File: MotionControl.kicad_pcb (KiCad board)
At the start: 2 copper layers, 29 parts, among them J1 Screw_Terminal_01x02, J2 Conn_ARM_JTAG_SWD_10, P1 USB_C_Plug_USB2.0, SW1 SW_Push, U1 ATSAMD21J18A-A, U2 AP2112K-3.3, Y1 32.768kHz

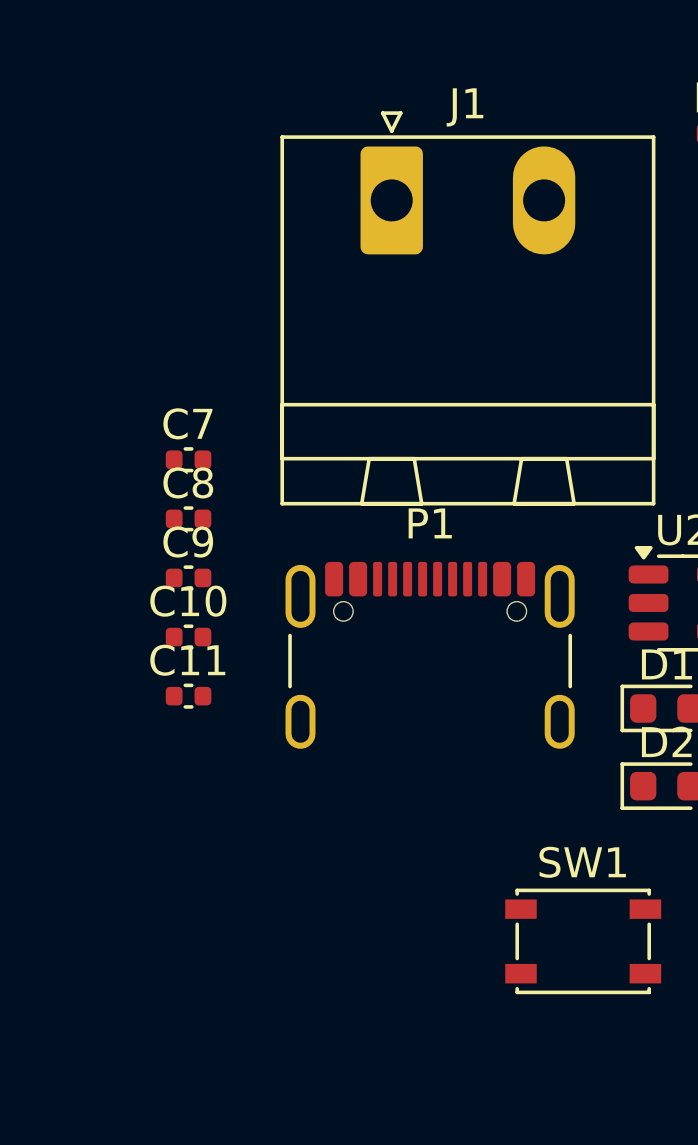
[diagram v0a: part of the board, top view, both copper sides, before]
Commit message: tx, rx leds
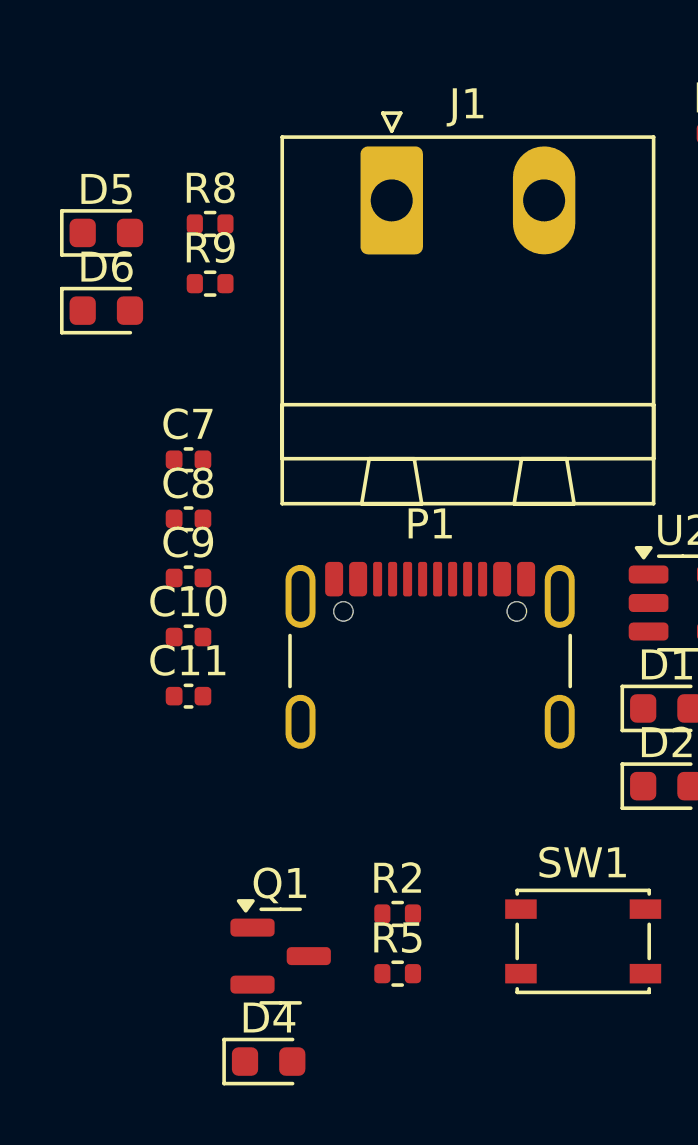
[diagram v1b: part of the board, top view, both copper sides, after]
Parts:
- added D4: Blue, LED_SMD:LED_0603_1608Metric, F.Cu at (125.4, 123.7)
- added D5: Green, LED_SMD:LED_0603_1608Metric, F.Cu at (120.0, 96.1)
- added D6: Yellow, LED_SMD:LED_0603_1608Metric, F.Cu at (120.0, 98.7)
- added Q1: 2N7002, Package_TO_SOT_SMD:SOT-23, F.Cu at (125.8, 120.2)
- added R2: 10R, Resistor_SMD:R_0402_1005Metric, F.Cu at (129.7, 118.8)
- added R5: 100K, Resistor_SMD:R_0402_1005Metric, F.Cu at (129.7, 120.8)
- added R8: 130R, Resistor_SMD:R_0402_1005Metric, F.Cu at (123.5, 95.8)
- added R9: 130R, Resistor_SMD:R_0402_1005Metric, F.Cu at (123.5, 97.8)
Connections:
- U1 pad 36: unconnected-(U1-PA17-Pad36) -> PA17_LED
- U1 pad 51: unconnected-(U1-PA27-Pad51) -> PA27_TX_LED
- U1 pad 64: unconnected-(U1-PB03-Pad64) -> PB03_RX_LED

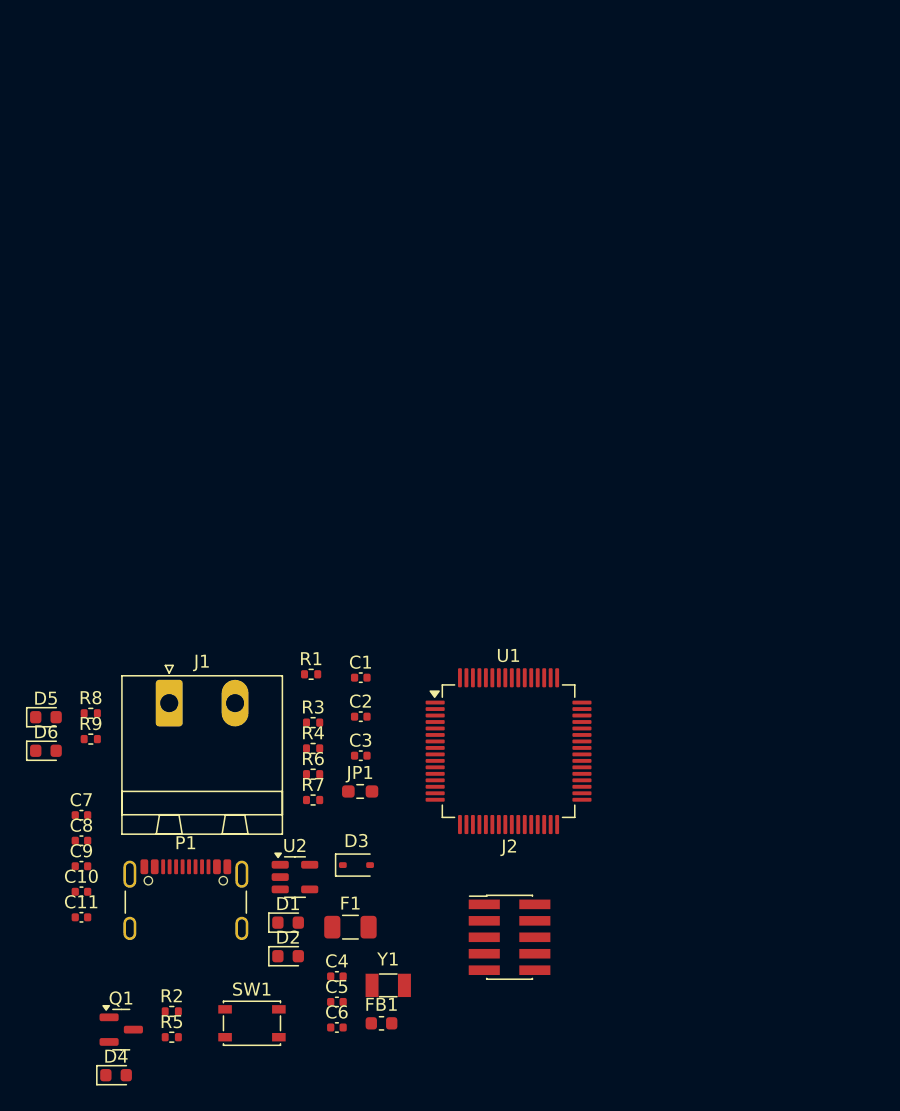
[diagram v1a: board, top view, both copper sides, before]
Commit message: Stepper unit
Made first revision for stepper unit
Contains TMC5160, Status LED, FETs, and complementary comps
Will be x4 later
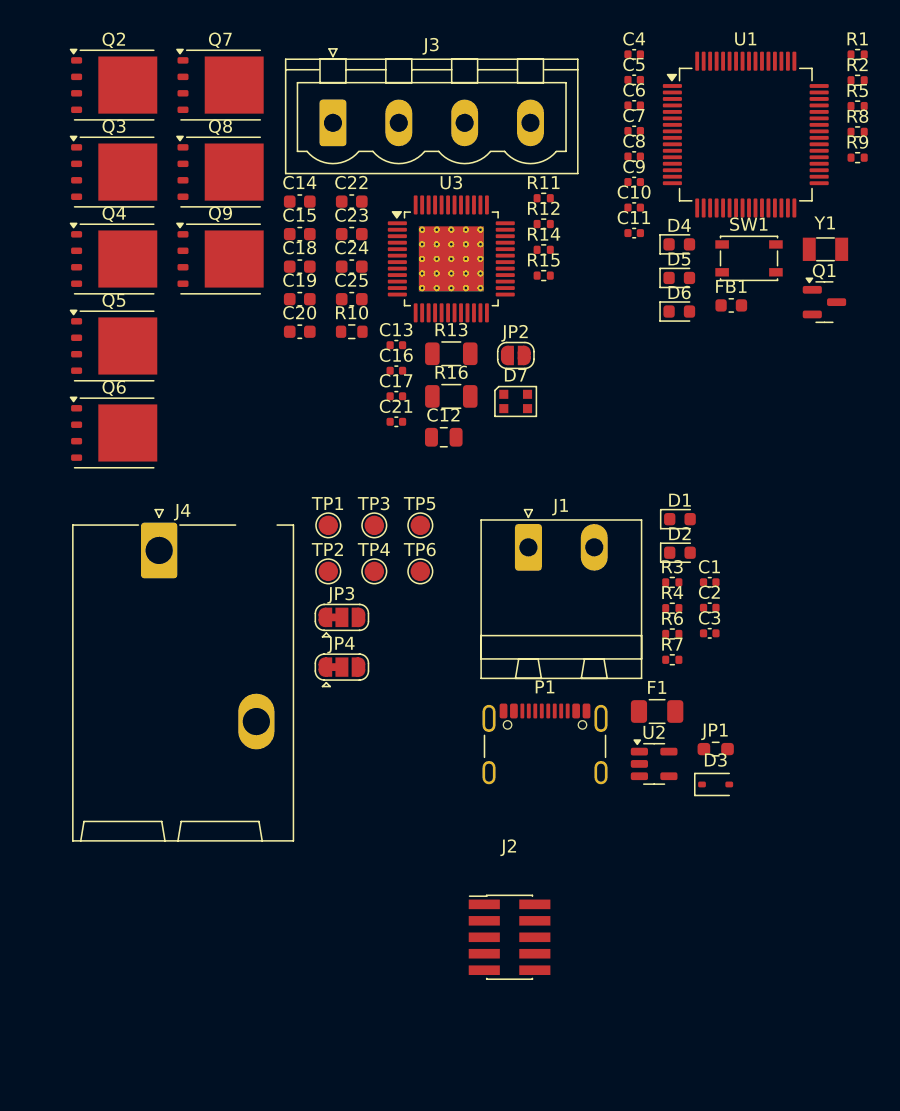
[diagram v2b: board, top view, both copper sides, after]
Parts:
- added C12: 10uF 50V, Capacitor_SMD:C_0805_2012Metric, F.Cu at (150.7, 74.5)
- added C13: 22nF 50V, Capacitor_SMD:C_0402_1005Metric, F.Cu at (147.1, 67.4)
- added C14: 100nF 50V, Capacitor_SMD:C_0603_1608Metric, F.Cu at (139.6, 56.3)
- added C15: 100nF 50V, Capacitor_SMD:C_0603_1608Metric, F.Cu at (139.6, 58.8)
- added C16: 470nF 10V, Capacitor_SMD:C_0402_1005Metric, F.Cu at (147.1, 69.3)
- added C17: 4.7uF 6.3V, Capacitor_SMD:C_0402_1005Metric, F.Cu at (147.1, 71.3)
- added C18: 2.2uF 25V, Capacitor_SMD:C_0603_1608Metric, F.Cu at (139.6, 61.3)
- added C19: 100nF 50V, Capacitor_SMD:C_0603_1608Metric, F.Cu at (139.6, 63.8)
- added C20: 100nF 50V, Capacitor_SMD:C_0603_1608Metric, F.Cu at (139.6, 66.3)
- added C21: 0.1uF, Capacitor_SMD:C_0402_1005Metric, F.Cu at (147.1, 73.3)
- added C22: 100nF 50V, Capacitor_SMD:C_0603_1608Metric, F.Cu at (143.6, 56.3)
- added C23: 100nF 50V, Capacitor_SMD:C_0603_1608Metric, F.Cu at (143.6, 58.8)
- added C24: 100nF 50V, Capacitor_SMD:C_0603_1608Metric, F.Cu at (143.6, 61.3)
- added C25: 100nF 50V, Capacitor_SMD:C_0603_1608Metric, F.Cu at (143.6, 63.8)
- added D7: WS2812B-2020, LED_SMD:LED_WS2812B-2020_PLCC4_2.0x2.0mm, F.Cu at (156.3, 71.7)
- added J3: Screw_Terminal_01x04, Connector_Phoenix_MSTB:PhoenixContact_MSTBVA_2,5_4-G-5,08_1x04_P5.08mm_Vertical, F.Cu at (142.2, 50.2)
- added J4: Screw_Terminal_01x02, Connector_Phoenix_SPT:PhoenixContact_SPT_5_2-H-7.5-ZB_1x02_P7.5mm_Horizontal, F.Cu at (128.8, 83.2)
- added JP2: Jumper_2, Jumper:SolderJumper-2_P1.3mm_Open_RoundedPad1.0x1.5mm, F.Cu at (156.3, 68.2)
- added JP3: SolderJumper_3_Bridged12, Jumper:SolderJumper-3_P1.3mm_Bridged12_RoundedPad1.0x1.5mm, F.Cu at (142.9, 88.4)
- added JP4: SolderJumper_3_Bridged12, Jumper:SolderJumper-3_P1.3mm_Bridged12_RoundedPad1.0x1.5mm, F.Cu at (142.9, 92.2)
- added Q2: CSD18533Q5A, Package_TO_SOT_SMD:TDSON-8-1, F.Cu at (125.3, 47.3)
- added Q3: CSD18533Q5A, Package_TO_SOT_SMD:TDSON-8-1, F.Cu at (125.3, 54.0)
- added Q4: CSD18533Q5A, Package_TO_SOT_SMD:TDSON-8-1, F.Cu at (125.3, 60.7)
- added Q5: CSD18533Q5A, Package_TO_SOT_SMD:TDSON-8-1, F.Cu at (125.3, 67.4)
- added Q6: CSD18533Q5A, Package_TO_SOT_SMD:TDSON-8-1, F.Cu at (125.3, 74.1)
- added Q7: CSD18533Q5A, Package_TO_SOT_SMD:TDSON-8-1, F.Cu at (133.5, 47.3)
- added Q8: CSD18533Q5A, Package_TO_SOT_SMD:TDSON-8-1, F.Cu at (133.5, 54.0)
- added Q9: CSD18533Q5A, Package_TO_SOT_SMD:TDSON-8-1, F.Cu at (133.5, 60.7)
- added R10: 2R, Resistor_SMD:R_0603_1608Metric, F.Cu at (143.6, 66.3)
- added R11: 47R, Resistor_SMD:R_0402_1005Metric, F.Cu at (158.4, 56.0)
- added R12: 47R, Resistor_SMD:R_0402_1005Metric, F.Cu at (158.4, 58.0)
- added R13: R, Resistor_SMD:R_1206_3216Metric, F.Cu at (151.3, 68.0)
- added R14: 47R, Resistor_SMD:R_0402_1005Metric, F.Cu at (158.4, 60.0)
- added R15: 47R, Resistor_SMD:R_0402_1005Metric, F.Cu at (158.4, 62.0)
- added R16: R, Resistor_SMD:R_1206_3216Metric, F.Cu at (151.3, 71.3)
- added TP1: TestPoint, TestPoint:TestPoint_Pad_D1.5mm, F.Cu at (141.8, 81.3)
- added TP2: TestPoint, TestPoint:TestPoint_Pad_D1.5mm, F.Cu at (141.8, 84.8)
- added TP3: TestPoint, TestPoint:TestPoint_Pad_D1.5mm, F.Cu at (145.4, 81.3)
- added TP4: TestPoint, TestPoint:TestPoint_Pad_D1.5mm, F.Cu at (145.4, 84.8)
- added TP5: TestPoint, TestPoint:TestPoint_Pad_D1.5mm, F.Cu at (148.9, 81.3)
- added TP6: TestPoint, TestPoint:TestPoint_Pad_D1.5mm, F.Cu at (148.9, 84.8)
- added U3: TMC5160A-TA, Package_QFP:TQFP-48-1EP_7x7mm_P0.5mm_EP5x5mm_ThermalVias, F.Cu at (151.3, 60.7)
- moved R2 89.2 mm to (182.7, 46.9)
- moved R5 89.2 mm to (182.7, 48.9)
- moved Q1 78.1 mm to (180.1, 64.0)
- moved D4 77.4 mm to (168.9, 59.6)
- moved C4 74.7 mm to (165.4, 44.9)
- moved C5 74.7 mm to (165.4, 46.9)
- moved C6 74.7 mm to (165.4, 48.9)
- moved R8 74.2 mm to (182.7, 50.9)
- moved R9 74.2 mm to (182.7, 52.9)
- moved SW1 70.4 mm to (174.3, 60.7)
- moved C7 67.9 mm to (165.4, 50.8)
- moved C8 67.9 mm to (165.4, 52.8)
- moved C10 67.9 mm to (165.4, 56.7)
- moved C11 67.9 mm to (165.4, 58.7)
- moved C9 67.9 mm to (165.4, 54.8)
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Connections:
- Q1 pad 2: Net-(D4-K) -> GND
- Q1 pad 3: GND -> Net-(D4-K)

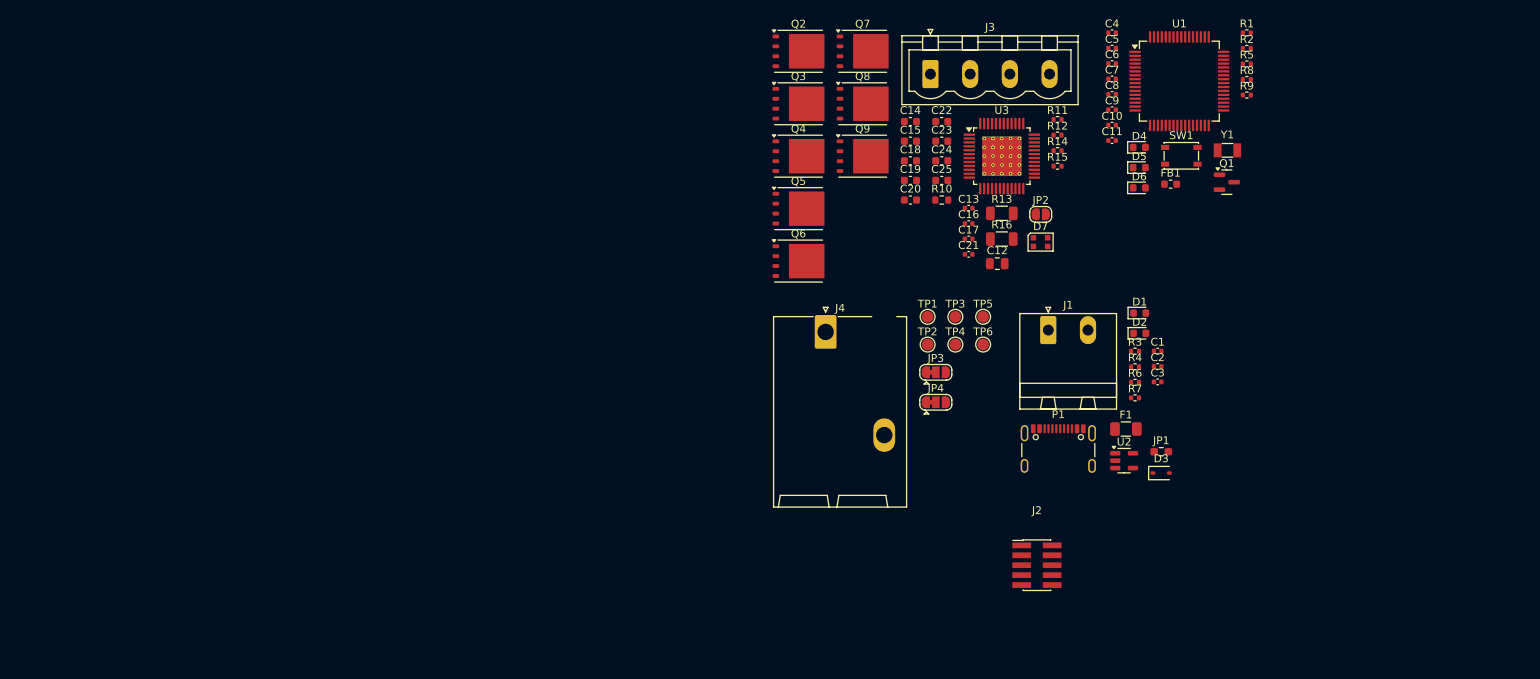
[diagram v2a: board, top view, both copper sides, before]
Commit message: x4 stepper units
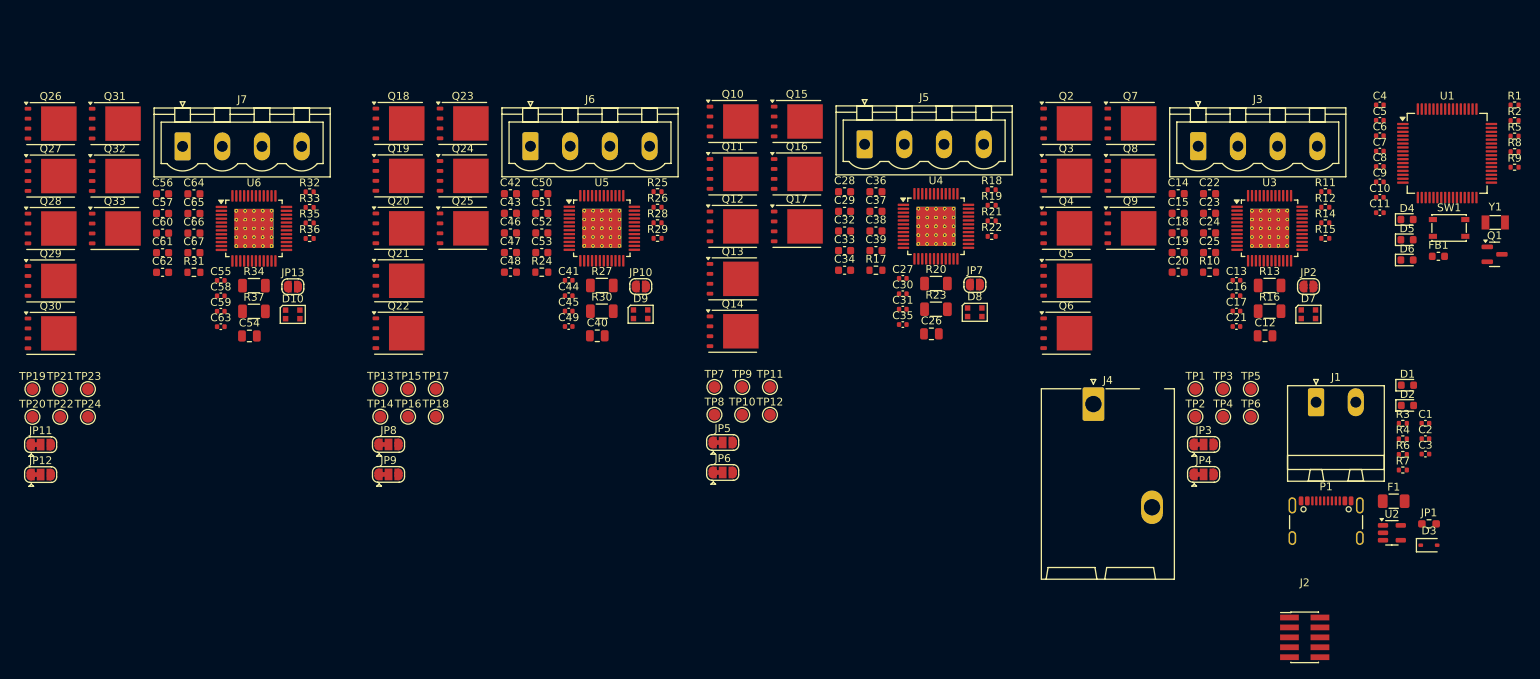
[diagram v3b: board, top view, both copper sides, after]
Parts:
- added C26: 10uF 50V, Capacitor_SMD:C_0805_2012Metric, F.Cu at (142.3, 83.4)
- added C27: 22nF 50V, Capacitor_SMD:C_0402_1005Metric, F.Cu at (138.6, 76.3)
- added C28: 100nF 50V, Capacitor_SMD:C_0603_1608Metric, F.Cu at (131.2, 65.3)
- added C29: 100nF 50V, Capacitor_SMD:C_0603_1608Metric, F.Cu at (131.2, 67.8)
- added C30: 470nF 10V, Capacitor_SMD:C_0402_1005Metric, F.Cu at (138.6, 78.3)
- added C31: 4.7uF 6.3V, Capacitor_SMD:C_0402_1005Metric, F.Cu at (138.6, 80.3)
- added C32: 2.2uF 25V, Capacitor_SMD:C_0603_1608Metric, F.Cu at (131.2, 70.3)
- added C33: 100nF 50V, Capacitor_SMD:C_0603_1608Metric, F.Cu at (131.2, 72.8)
- added C34: 100nF 50V, Capacitor_SMD:C_0603_1608Metric, F.Cu at (131.2, 75.3)
- added C35: 0.1uF, Capacitor_SMD:C_0402_1005Metric, F.Cu at (138.6, 82.2)
- added C36: 100nF 50V, Capacitor_SMD:C_0603_1608Metric, F.Cu at (135.2, 65.3)
- added C37: 100nF 50V, Capacitor_SMD:C_0603_1608Metric, F.Cu at (135.2, 67.8)
- added C38: 100nF 50V, Capacitor_SMD:C_0603_1608Metric, F.Cu at (135.2, 70.3)
- added C39: 100nF 50V, Capacitor_SMD:C_0603_1608Metric, F.Cu at (135.2, 72.8)
- added C40: 10uF 50V, Capacitor_SMD:C_0805_2012Metric, F.Cu at (99.5, 83.7)
- added C41: 22nF 50V, Capacitor_SMD:C_0402_1005Metric, F.Cu at (95.9, 76.6)
- added C42: 100nF 50V, Capacitor_SMD:C_0603_1608Metric, F.Cu at (88.4, 65.5)
- added C43: 100nF 50V, Capacitor_SMD:C_0603_1608Metric, F.Cu at (88.4, 68.0)
- added C44: 470nF 10V, Capacitor_SMD:C_0402_1005Metric, F.Cu at (95.9, 78.6)
- added C45: 4.7uF 6.3V, Capacitor_SMD:C_0402_1005Metric, F.Cu at (95.9, 80.5)
- added C46: 2.2uF 25V, Capacitor_SMD:C_0603_1608Metric, F.Cu at (88.4, 70.5)
- added C47: 100nF 50V, Capacitor_SMD:C_0603_1608Metric, F.Cu at (88.4, 73.0)
- added C48: 100nF 50V, Capacitor_SMD:C_0603_1608Metric, F.Cu at (88.4, 75.5)
- added C49: 0.1uF, Capacitor_SMD:C_0402_1005Metric, F.Cu at (95.9, 82.5)
- added C50: 100nF 50V, Capacitor_SMD:C_0603_1608Metric, F.Cu at (92.5, 65.5)
- added C51: 100nF 50V, Capacitor_SMD:C_0603_1608Metric, F.Cu at (92.5, 68.0)
- added C52: 100nF 50V, Capacitor_SMD:C_0603_1608Metric, F.Cu at (92.5, 70.5)
- added C53: 100nF 50V, Capacitor_SMD:C_0603_1608Metric, F.Cu at (92.5, 73.0)
- added C54: 10uF 50V, Capacitor_SMD:C_0805_2012Metric, F.Cu at (55.0, 83.7)
- added C55: 22nF 50V, Capacitor_SMD:C_0402_1005Metric, F.Cu at (51.4, 76.6)
- added C56: 100nF 50V, Capacitor_SMD:C_0603_1608Metric, F.Cu at (43.9, 65.5)
- added C57: 100nF 50V, Capacitor_SMD:C_0603_1608Metric, F.Cu at (43.9, 68.0)
- added C58: 470nF 10V, Capacitor_SMD:C_0402_1005Metric, F.Cu at (51.4, 78.6)
- added C59: 4.7uF 6.3V, Capacitor_SMD:C_0402_1005Metric, F.Cu at (51.4, 80.5)
- added C60: 2.2uF 25V, Capacitor_SMD:C_0603_1608Metric, F.Cu at (43.9, 70.5)
- added C61: 100nF 50V, Capacitor_SMD:C_0603_1608Metric, F.Cu at (43.9, 73.1)
- added C62: 100nF 50V, Capacitor_SMD:C_0603_1608Metric, F.Cu at (43.9, 75.6)
- added C63: 0.1uF, Capacitor_SMD:C_0402_1005Metric, F.Cu at (51.4, 82.5)
- added C64: 100nF 50V, Capacitor_SMD:C_0603_1608Metric, F.Cu at (47.9, 65.5)
- added C65: 100nF 50V, Capacitor_SMD:C_0603_1608Metric, F.Cu at (47.9, 68.0)
- added C66: 100nF 50V, Capacitor_SMD:C_0603_1608Metric, F.Cu at (47.9, 70.5)
- added C67: 100nF 50V, Capacitor_SMD:C_0603_1608Metric, F.Cu at (47.9, 73.1)
- added D10: WS2812B-2020, LED_SMD:LED_WS2812B-2020_PLCC4_2.0x2.0mm, F.Cu at (60.6, 81.0)
- added D8: WS2812B-2020, LED_SMD:LED_WS2812B-2020_PLCC4_2.0x2.0mm, F.Cu at (147.8, 80.7)
- added D9: WS2812B-2020, LED_SMD:LED_WS2812B-2020_PLCC4_2.0x2.0mm, F.Cu at (105.1, 80.9)
- added J5: Screw_Terminal_01x04, Connector_Phoenix_MSTB:PhoenixContact_MSTBVA_2,5_4-G-5,08_1x04_P5.08mm_Vertical, F.Cu at (133.8, 59.2)
- added J6: Screw_Terminal_01x04, Connector_Phoenix_MSTB:PhoenixContact_MSTBVA_2,5_4-G-5,08_1x04_P5.08mm_Vertical, F.Cu at (91.0, 59.4)
- added J7: Screw_Terminal_01x04, Connector_Phoenix_MSTB:PhoenixContact_MSTBVA_2,5_4-G-5,08_1x04_P5.08mm_Vertical, F.Cu at (46.5, 59.5)
- added JP10: Jumper_2, Jumper:SolderJumper-2_P1.3mm_Open_RoundedPad1.0x1.5mm, F.Cu at (105.1, 77.4)
- added JP11: SolderJumper_3_Bridged12, Jumper:SolderJumper-3_P1.3mm_Bridged12_RoundedPad1.0x1.5mm, F.Cu at (28.3, 97.6)
- added JP12: SolderJumper_3_Bridged12, Jumper:SolderJumper-3_P1.3mm_Bridged12_RoundedPad1.0x1.5mm, F.Cu at (28.3, 101.4)
- added JP13: Jumper_2, Jumper:SolderJumper-2_P1.3mm_Open_RoundedPad1.0x1.5mm, F.Cu at (60.6, 77.4)
- added JP5: SolderJumper_3_Bridged12, Jumper:SolderJumper-3_P1.3mm_Bridged12_RoundedPad1.0x1.5mm, F.Cu at (115.6, 97.3)
- added JP6: SolderJumper_3_Bridged12, Jumper:SolderJumper-3_P1.3mm_Bridged12_RoundedPad1.0x1.5mm, F.Cu at (115.6, 101.2)
- added JP7: Jumper_2, Jumper:SolderJumper-2_P1.3mm_Open_RoundedPad1.0x1.5mm, F.Cu at (147.9, 77.1)
- added JP8: SolderJumper_3_Bridged12, Jumper:SolderJumper-3_P1.3mm_Bridged12_RoundedPad1.0x1.5mm, F.Cu at (72.8, 97.6)
- added JP9: SolderJumper_3_Bridged12, Jumper:SolderJumper-3_P1.3mm_Bridged12_RoundedPad1.0x1.5mm, F.Cu at (72.8, 101.4)
- added Q10: CSD18533Q5A, Package_TO_SOT_SMD:TDSON-8-1, F.Cu at (116.9, 56.3)
- added Q11: CSD18533Q5A, Package_TO_SOT_SMD:TDSON-8-1, F.Cu at (116.9, 63.0)
- added Q12: CSD18533Q5A, Package_TO_SOT_SMD:TDSON-8-1, F.Cu at (116.9, 69.7)
- added Q13: CSD18533Q5A, Package_TO_SOT_SMD:TDSON-8-1, F.Cu at (116.9, 76.4)
- added Q14: CSD18533Q5A, Package_TO_SOT_SMD:TDSON-8-1, F.Cu at (116.9, 83.1)
- added Q15: CSD18533Q5A, Package_TO_SOT_SMD:TDSON-8-1, F.Cu at (125.1, 56.3)
- added Q16: CSD18533Q5A, Package_TO_SOT_SMD:TDSON-8-1, F.Cu at (125.1, 63.0)
- added Q17: CSD18533Q5A, Package_TO_SOT_SMD:TDSON-8-1, F.Cu at (125.1, 69.7)
- added Q18: CSD18533Q5A, Package_TO_SOT_SMD:TDSON-8-1, F.Cu at (74.1, 56.5)
- added Q19: CSD18533Q5A, Package_TO_SOT_SMD:TDSON-8-1, F.Cu at (74.1, 63.2)
- added Q20: CSD18533Q5A, Package_TO_SOT_SMD:TDSON-8-1, F.Cu at (74.1, 69.9)
- added Q21: CSD18533Q5A, Package_TO_SOT_SMD:TDSON-8-1, F.Cu at (74.1, 76.7)
- added Q22: CSD18533Q5A, Package_TO_SOT_SMD:TDSON-8-1, F.Cu at (74.1, 83.4)
- added Q23: CSD18533Q5A, Package_TO_SOT_SMD:TDSON-8-1, F.Cu at (82.3, 56.5)
- added Q24: CSD18533Q5A, Package_TO_SOT_SMD:TDSON-8-1, F.Cu at (82.3, 63.2)
- added Q25: CSD18533Q5A, Package_TO_SOT_SMD:TDSON-8-1, F.Cu at (82.3, 69.9)
- added Q26: CSD18533Q5A, Package_TO_SOT_SMD:TDSON-8-1, F.Cu at (29.6, 56.5)
- added Q27: CSD18533Q5A, Package_TO_SOT_SMD:TDSON-8-1, F.Cu at (29.6, 63.2)
- added Q28: CSD18533Q5A, Package_TO_SOT_SMD:TDSON-8-1, F.Cu at (29.6, 70.0)
- added Q29: CSD18533Q5A, Package_TO_SOT_SMD:TDSON-8-1, F.Cu at (29.6, 76.7)
- added Q30: CSD18533Q5A, Package_TO_SOT_SMD:TDSON-8-1, F.Cu at (29.6, 83.4)
- added Q31: CSD18533Q5A, Package_TO_SOT_SMD:TDSON-8-1, F.Cu at (37.8, 56.5)
- added Q32: CSD18533Q5A, Package_TO_SOT_SMD:TDSON-8-1, F.Cu at (37.8, 63.2)
- added Q33: CSD18533Q5A, Package_TO_SOT_SMD:TDSON-8-1, F.Cu at (37.8, 70.0)
- added R17: 2R, Resistor_SMD:R_0603_1608Metric, F.Cu at (135.2, 75.3)
- added R18: 47R, Resistor_SMD:R_0402_1005Metric, F.Cu at (150.0, 65.0)
- added R19: 47R, Resistor_SMD:R_0402_1005Metric, F.Cu at (150.0, 67.0)
- added R20: R, Resistor_SMD:R_1206_3216Metric, F.Cu at (142.9, 77.0)
- added R21: 47R, Resistor_SMD:R_0402_1005Metric, F.Cu at (150.0, 69.0)
- added R22: 47R, Resistor_SMD:R_0402_1005Metric, F.Cu at (150.0, 71.0)
- added R23: R, Resistor_SMD:R_1206_3216Metric, F.Cu at (142.9, 80.3)
- added R24: 2R, Resistor_SMD:R_0603_1608Metric, F.Cu at (92.5, 75.5)
- added R25: 47R, Resistor_SMD:R_0402_1005Metric, F.Cu at (107.3, 65.2)
- added R26: 47R, Resistor_SMD:R_0402_1005Metric, F.Cu at (107.3, 67.2)
- added R27: R, Resistor_SMD:R_1206_3216Metric, F.Cu at (100.1, 77.2)
- added R28: 47R, Resistor_SMD:R_0402_1005Metric, F.Cu at (107.3, 69.2)
- added R29: 47R, Resistor_SMD:R_0402_1005Metric, F.Cu at (107.3, 71.2)
- added R30: R, Resistor_SMD:R_1206_3216Metric, F.Cu at (100.1, 80.5)
- added R31: 2R, Resistor_SMD:R_0603_1608Metric, F.Cu at (47.9, 75.6)
- added R32: 47R, Resistor_SMD:R_0402_1005Metric, F.Cu at (62.8, 65.3)
- added R33: 47R, Resistor_SMD:R_0402_1005Metric, F.Cu at (62.8, 67.3)
- added R34: R, Resistor_SMD:R_1206_3216Metric, F.Cu at (55.6, 77.3)
- added R35: 47R, Resistor_SMD:R_0402_1005Metric, F.Cu at (62.8, 69.2)
- added R36: 47R, Resistor_SMD:R_0402_1005Metric, F.Cu at (62.8, 71.2)
- added R37: R, Resistor_SMD:R_1206_3216Metric, F.Cu at (55.6, 80.6)
- added TP10: TestPoint, TestPoint:TestPoint_Pad_D1.5mm, F.Cu at (118.1, 93.8)
- added TP11: TestPoint, TestPoint:TestPoint_Pad_D1.5mm, F.Cu at (121.6, 90.2)
- added TP12: TestPoint, TestPoint:TestPoint_Pad_D1.5mm, F.Cu at (121.6, 93.8)
- added TP13: TestPoint, TestPoint:TestPoint_Pad_D1.5mm, F.Cu at (71.8, 90.5)
- added TP14: TestPoint, TestPoint:TestPoint_Pad_D1.5mm, F.Cu at (71.8, 94.0)
- added TP15: TestPoint, TestPoint:TestPoint_Pad_D1.5mm, F.Cu at (75.3, 90.5)
- added TP16: TestPoint, TestPoint:TestPoint_Pad_D1.5mm, F.Cu at (75.3, 94.0)
- added TP17: TestPoint, TestPoint:TestPoint_Pad_D1.5mm, F.Cu at (78.9, 90.5)
- added TP18: TestPoint, TestPoint:TestPoint_Pad_D1.5mm, F.Cu at (78.9, 94.0)
- added TP19: TestPoint, TestPoint:TestPoint_Pad_D1.5mm, F.Cu at (27.3, 90.5)
- added TP20: TestPoint, TestPoint:TestPoint_Pad_D1.5mm, F.Cu at (27.3, 94.1)
- added TP21: TestPoint, TestPoint:TestPoint_Pad_D1.5mm, F.Cu at (30.8, 90.5)
- added TP22: TestPoint, TestPoint:TestPoint_Pad_D1.5mm, F.Cu at (30.8, 94.1)
- added TP23: TestPoint, TestPoint:TestPoint_Pad_D1.5mm, F.Cu at (34.4, 90.5)
- added TP24: TestPoint, TestPoint:TestPoint_Pad_D1.5mm, F.Cu at (34.4, 94.1)
- added TP7: TestPoint, TestPoint:TestPoint_Pad_D1.5mm, F.Cu at (114.5, 90.2)
- added TP8: TestPoint, TestPoint:TestPoint_Pad_D1.5mm, F.Cu at (114.5, 93.8)
- added TP9: TestPoint, TestPoint:TestPoint_Pad_D1.5mm, F.Cu at (118.1, 90.2)
- added U4: TMC5160A-TA, Package_QFP:TQFP-48-1EP_7x7mm_P0.5mm_EP5x5mm_ThermalVias, F.Cu at (142.9, 69.7)
- added U5: TMC5160A-TA, Package_QFP:TQFP-48-1EP_7x7mm_P0.5mm_EP5x5mm_ThermalVias, F.Cu at (100.1, 69.9)
- added U6: TMC5160A-TA, Package_QFP:TQFP-48-1EP_7x7mm_P0.5mm_EP5x5mm_ThermalVias, F.Cu at (55.6, 70.0)
- moved C10 35.5 mm to (199.7, 66.0)
- moved C11 35.5 mm to (199.7, 67.9)
- moved C12 35.5 mm to (185.0, 83.7)
- moved C4 35.5 mm to (199.7, 54.1)
- moved C5 35.5 mm to (199.7, 56.1)
- moved C6 35.5 mm to (199.7, 58.1)
- moved C7 35.5 mm to (199.7, 60.1)
- moved C8 35.5 mm to (199.7, 62.0)
- moved C9 35.5 mm to (199.7, 64.0)
- moved D1 35.5 mm to (203.2, 90.0)
- moved D2 35.5 mm to (203.2, 92.6)
- moved D3 35.5 mm to (206.0, 110.5)
- moved J4 35.5 mm to (163.0, 92.4)
- moved R3 35.5 mm to (202.6, 94.9)
- moved R4 35.5 mm to (202.6, 96.9)
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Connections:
- net /Steppers/CSn renamed /Steppers/CSn1
- net /Steppers/LED renamed /Steppers/Stepper Unit/LED_IN
